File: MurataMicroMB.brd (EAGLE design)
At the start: 90 x 63 mm, 73 parts, among them CON1 CON_MICROSD_C2395, CON2 WM17143CT-ND, CON4 CON_MICROSD_C2395, IC3 IC_LPC11U35_QFN33_5X5, IC4 LDO4_3.3_SOT223, Q1 12M/3225, SW1 P-8073, SW2 P-8073, SW3 P-8073, X1 TSW-102-02-S-S

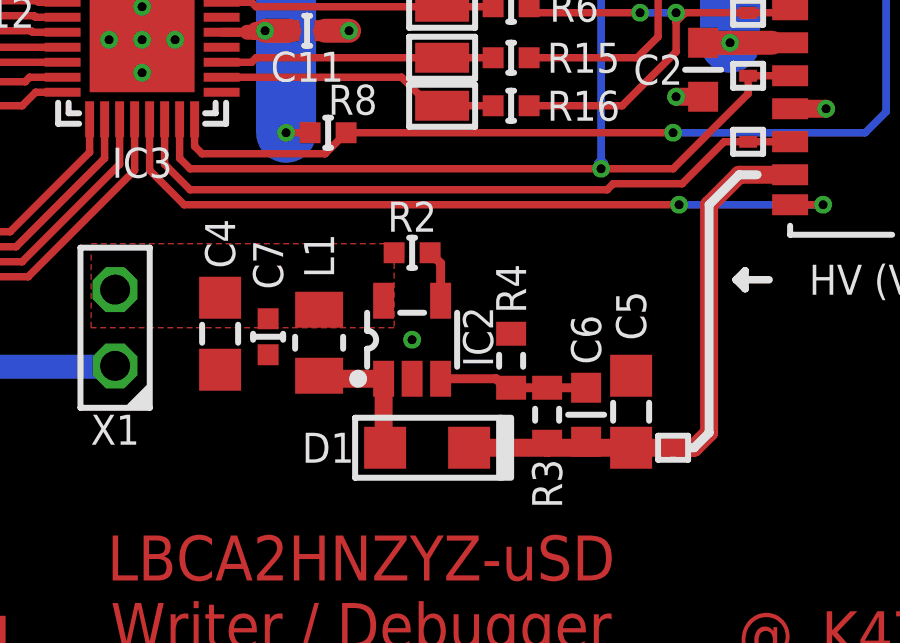
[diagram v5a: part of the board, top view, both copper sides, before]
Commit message: [ MB ] TP12;IC4;CON2
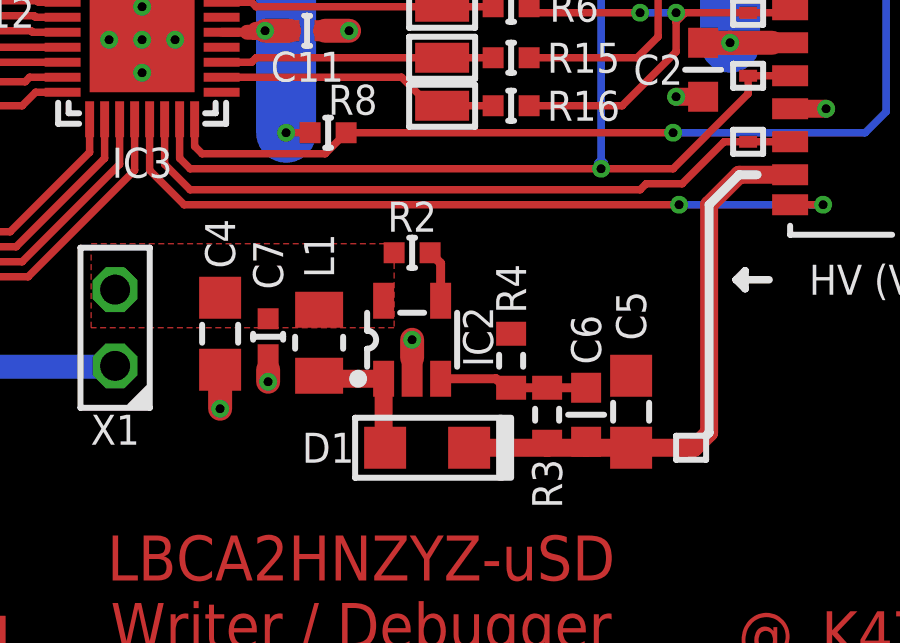
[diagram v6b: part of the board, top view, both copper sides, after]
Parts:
- IC4: value LDO4_3.3_SOT223 -> (none)
- moved TP12 0.60 mm to (60.3, 17.9)
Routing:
- net GND: track 11.8 -> 15.2 mm, vias 19 -> 21
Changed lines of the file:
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@@
 <wire x1="61.9" y1="27" x2="60.9" y2="26" width="0.3" layer="21"/>
 <wire x1="60.9" y1="26" x2="60.9" y2="18.4" width="0.3" layer="21"/>
-<wire x1="60.9" y1="18.4" x2="60.4" y2="17.9" width="0.3" layer="21"/>
-<wire x1="60.4" y1="17.9" x2="60.3" y2="17.9" width="0.3" layer="21"/>
 <rectangle x1="47.1" y1="21" x2="48.7" y2="21.8" layer="41"/>
 <wire x1="62.7" y1="26.4" x2="62.2" y2="26.4" width="0.2" layer="41"/>
@@
 <text x="50" y="48" size="1.2" layer="21" ratio="17" align="center">ISP</text>
 <text x="70" y="48" size="1.2" layer="21" ratio="17" align="center">!TARGET!</text>
+<wire x1="60.9" y1="18.4" x2="60.8" y2="18.3" width="0.3" layer="21"/>
 </plain>
 <attributes>
@@
 <attribute name="DIGIKEY" value="490-5858-1-ND" x="44.3" y="38.9" size="1.778" layer="27" rot="R90" display="off"/>
 </element>
-<element name="IC4" library="mylib" package="IC_SOT223" value="LDO4_3.3_SOT223" x="19.3" y="39.5" smashed="yes" rot="R270">
+<element name="IC4" library="mylib" package="IC_SOT223" value="" x="19.3" y="39.5" smashed="yes" rot="R270">
 <attribute name="NAME" x="19.3" y="43.6" size="1" layer="25" ratio="20" rot="R180" align="center"/>
 <attribute name="VALUE" x="19.8" y="42.8" size="1" layer="27" ratio="20" rot="R90"/>
@@
 <attribute name="DIGIKEY" value="36-5019CT-ND" x="77" y="20" size="1" layer="27" ratio="20" rot="R90" display="off"/>
 </element>
-<element name="TP12" library="mylib" package="TP06RECT" value="" x="59.7" y="17.9" smashed="yes" rot="R90">
-<attribute name="VALUE" x="60.081" y="17.646" size="0.0254" layer="27" rot="R90"/>
-<attribute name="NOT_COMPONENT" value="YES" x="59.7" y="17.9" size="1.778" layer="27" rot="R90" display="off"/>
+<element name="TP12" library="mylib" package="TP06RECT" value="" x="60.3" y="17.9" smashed="yes" rot="R90">
+<attribute name="VALUE" x="60.681" y="17.646" size="0.0254" layer="27" rot="R90"/>
+<attribute name="NOT_COMPONENT" value="YES" x="60.3" y="17.9" size="1.778" layer="27" rot="R90" display="off"/>
 </element>
 <element name="TP14" library="mylib" package="TP_4020" value="" x="13" y="20" rot="R90">
@@
 <contactref element="TP16" pad="TP"/>
 <contactref element="IC1" pad="3"/>
+<wire x1="51" y1="21.5" x2="51" y2="20.9" width="0.8" layer="1"/>
+<wire x1="51" y1="20.9" x2="51" y2="20.2" width="0.6" layer="1"/>
+<via x="46.2" y="20.1" extent="1-16" drill="0.3"/>
+<wire x1="46.2" y1="20.1" x2="46.2" y2="20.5" width="0.8" layer="1"/>
+<wire x1="46.2" y1="20.5" x2="46.2" y2="21" width="0.6" layer="1"/>
+<via x="44.6" y="19.2" extent="1-16" drill="0.3"/>
+<wire x1="44.6" y1="19.2" x2="44.6" y2="20.4" width="0.8" layer="1"/>
 </signal>
 <signal name="D-">
@@
 <wire x1="62.2" y1="28.1" x2="61.4" y2="28.1" width="0.25" layer="1"/>
 <wire x1="61.4" y1="28.1" x2="60" y2="26.7" width="0.25" layer="1"/>
-<wire x1="60" y1="26.7" x2="57.7" y2="26.7" width="0.25" layer="1"/>
-<wire x1="57.7" y1="26.7" x2="57.5" y2="26.5" width="0.25" layer="1"/>
-<wire x1="57.5" y1="26.5" x2="43.6" y2="26.5" width="0.25" layer="1"/>
+<wire x1="60" y1="26.7" x2="58.8" y2="26.7" width="0.25" layer="1"/>
+<wire x1="58.8" y1="26.7" x2="58.6" y2="26.5" width="0.25" layer="1"/>
+<wire x1="58.6" y1="26.5" x2="43.6" y2="26.5" width="0.25" layer="1"/>
 <wire x1="43.6" y1="26.5" x2="42.75" y2="27.35" width="0.25" layer="1"/>
 <contactref element="IC3" pad="22"/>
@@
 <wire x1="56.8" y1="18.1" x2="56.8" y2="17.9" width="0.6" layer="1"/>
 <wire x1="55.5" y1="18.1" x2="55.5" y2="17.9" width="0.6" layer="1"/>
-<wire x1="58.3" y1="17.9" x2="59.7" y2="17.9" width="0.6" layer="1"/>
-<wire x1="59.7" y1="17.9" x2="60.4" y2="17.9" width="0.6" layer="1"/>
+<wire x1="58.3" y1="17.9" x2="60.3" y2="17.9" width="0.6" layer="1"/>
+<wire x1="60.3" y1="17.9" x2="60.4" y2="17.9" width="0.6" layer="1"/>
 <wire x1="60.4" y1="17.9" x2="60.9" y2="18.4" width="0.6" layer="1"/>
 <wire x1="60.9" y1="18.4" x2="60.9" y2="26" width="0.6" layer="1"/>
